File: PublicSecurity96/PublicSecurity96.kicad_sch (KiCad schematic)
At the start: 239 parts, among them J1 USB_C_Receptacle_USB2.0, U1 XC6206PxxxMR, U2 SRV05-4, U3 RP2040, Y1 16MHz

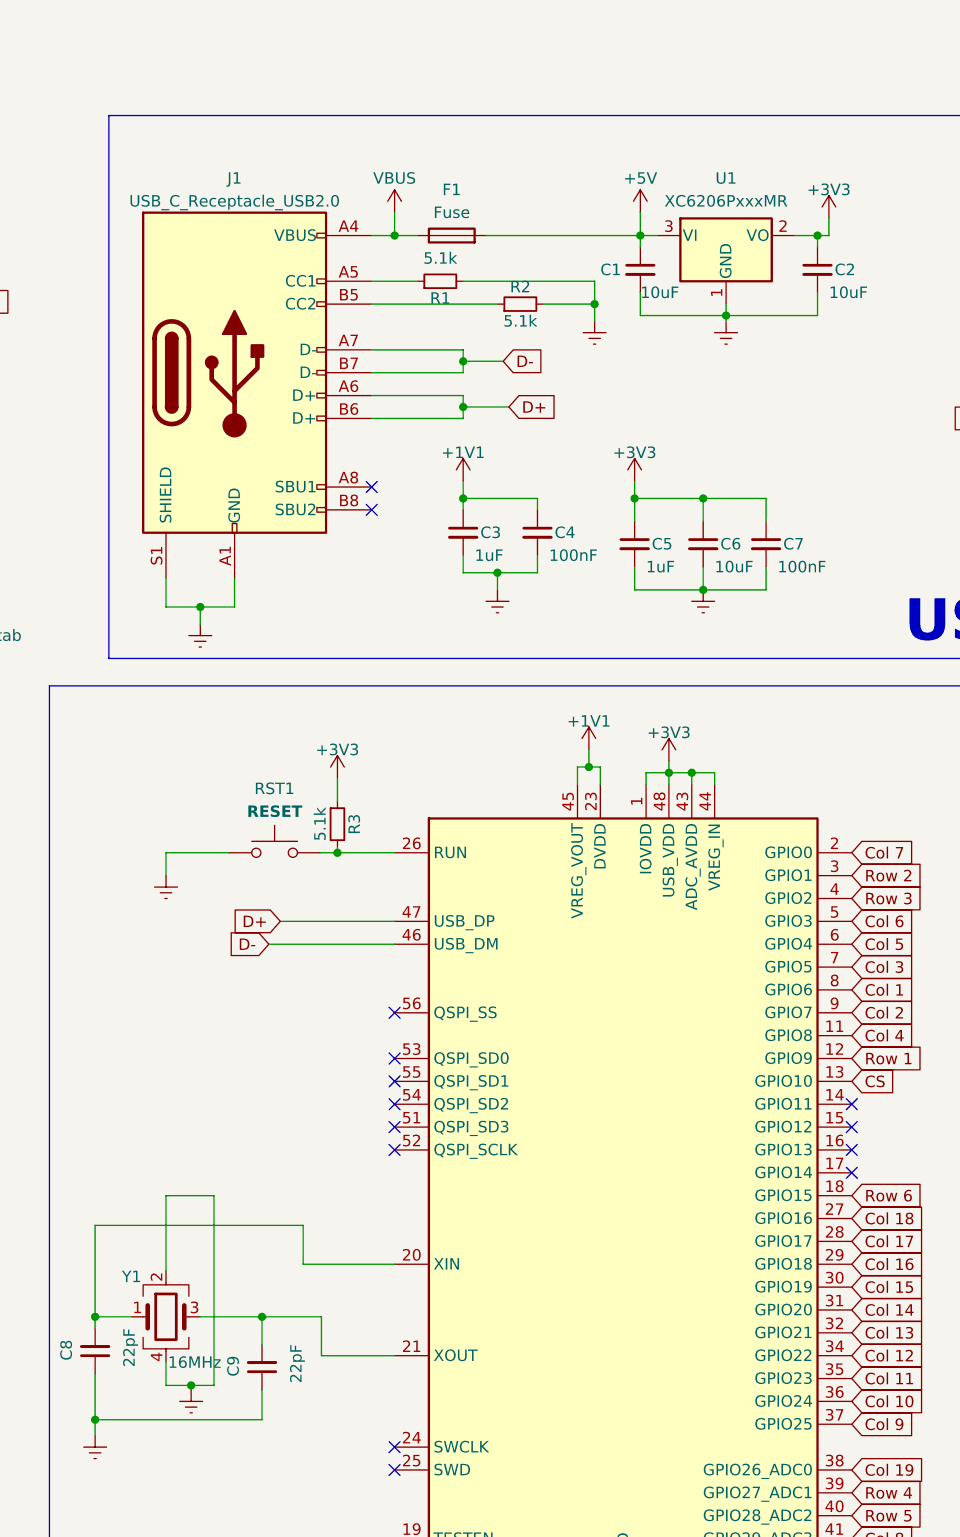
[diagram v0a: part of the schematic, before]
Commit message: kicad: swap U1 XC6206 -> AMS1117-3.3 (SOT-223 + C6186)
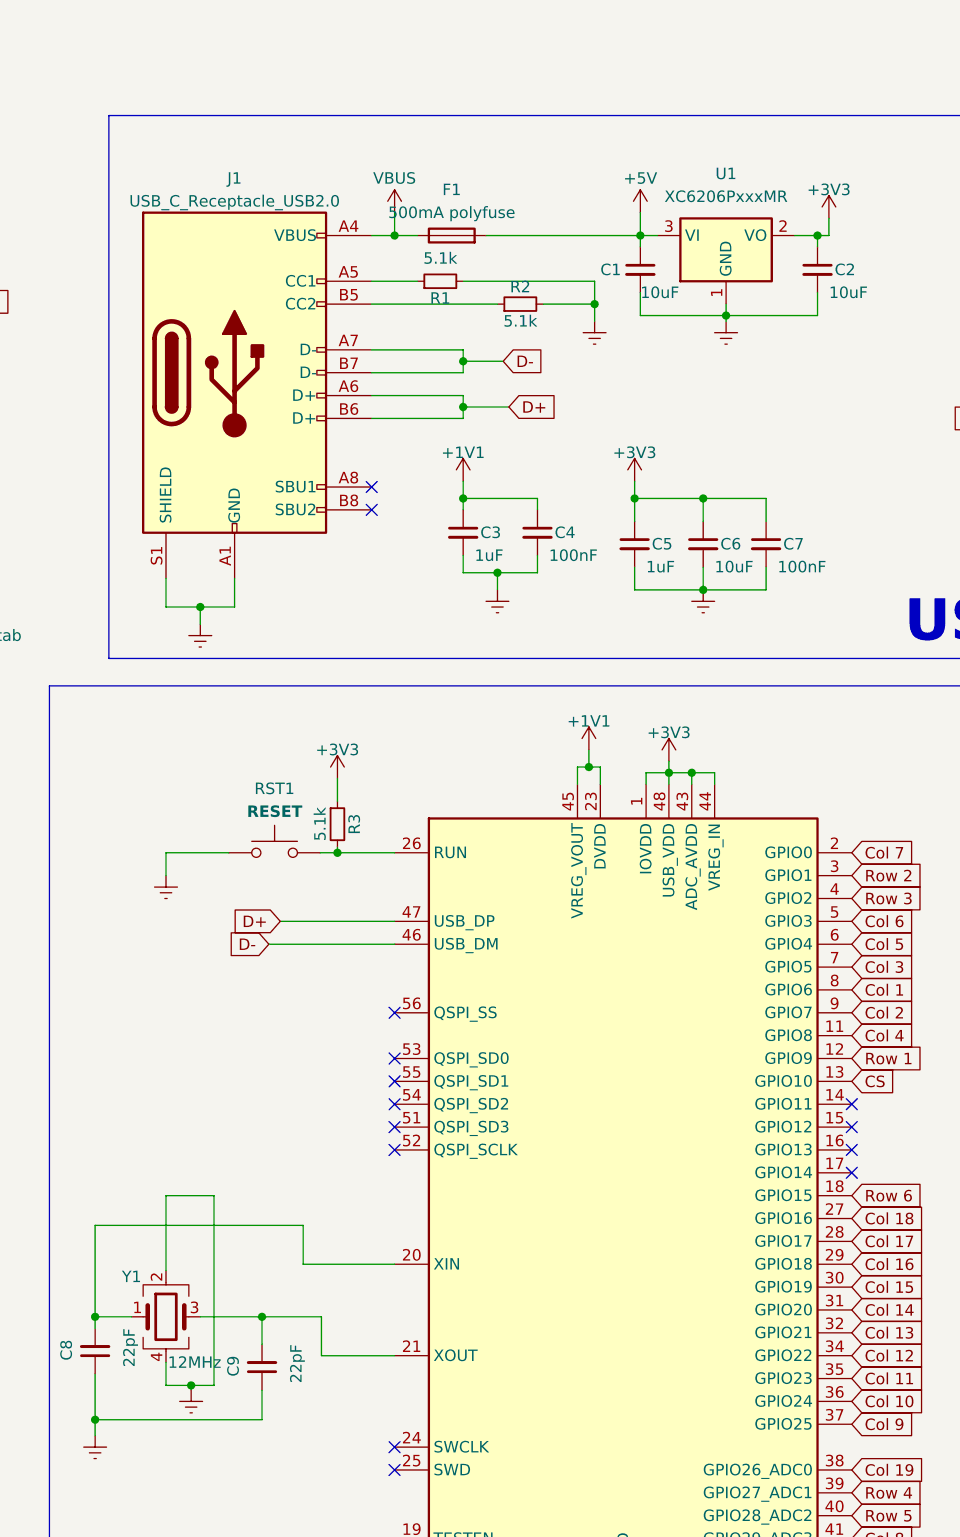
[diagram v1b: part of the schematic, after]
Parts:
- F1: value Fuse -> 500mA polyfuse; Comment 6V 500mA 100mA 1A 0805 Resettable Fuses ROHS -> 6V 500mA hold / 1A trip 1206 Resettable Polyfuse — VERIFY f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; JLCPCB part# C3035895 -> C2685389
- U1: symbol Regulator_Linear:XC6206PxxxMR -> Regulator_Linear:AMS1117-3.3; JLCPCB part# C15850 -> C6186
- Y1: value 16MHz -> 12MHz; Comment 8MHz 12pF ±10ppm SMD3225-4P Crystals ROHS -> 12MHz 12pF ±10ppm SMD3225-4P Crystals ROHS — VERIFY JLCPCB 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
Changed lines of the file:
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@@
 			)
 		)
-		(property "Value" "Fuse"
+		(property "Value" "500mA polyfuse"
 			(at 443.738 99.568 90)
 			(show_name no)
@@
 			)
 		)
-		(property "JLCPCB part#" " C3035895"
+		(property "JLCPCB part#" "C2685389"
 			(at 443.738 102.108 90)
 			(hide yes)
@@
 			)
 		)
-		(property "Comment" " 6V 500mA 100mA 1A 0805 Resettable Fuses ROHS"
+		(property "Comment" "6V 500mA hold / 1A trip 1206 Resettable Polyfuse — VERIFY footprint matches before fab"
 			(at 443.738 102.108 90)
 			(hide yes)
@@
 			)
 		)
-		(property "Value" "16MHz"
+		(property "Value" "12MHz"
 			(at 415.163 227.33 0)
 			(show_name no)
@@
 			)
 		)
-		(property "Comment" " 8MHz 12pF ±10ppm SMD3225-4P Crystals ROHS"
+		(property "Comment" " 12MHz 12pF ±10ppm SMD3225-4P Crystals ROHS — VERIFY JLCPCB part is 12MHz"
 			(at 411.988 222.25 0)
 			(hide yes)
@@
 	)
 	(symbol
-		(lib_id "Regulator_Linear:XC6206PxxxMR")
+		(lib_id "Regulator_Linear:AMS1117-3.3")
 		(at 474.218 102.108 0)
 		(unit 1)
@@
 		(fields_autoplaced yes)
 		(property "Reference" "U1"
-			(at 474.218 95.758 0)
+			(at 474.218 95.25 0)
 			(show_name no)
 			(do_not_autoplace no)
@@
 		)
 		(property "Value" "XC6206PxxxMR"
-			(at 474.218 98.298 0)
+			(at 474.218 97.79 0)
 			(show_name no)
 			(do_not_autoplace no)
@@
 		)
 		(property "Footprint" "Package_TO_SOT_SMD:SOT-223-3_TabPin2"
-			(at 474.218 96.393 0)
+			(at 474.218 97.028 0)
 			(hide yes)
 			(show_name no)
@@
 				(font
 					(size 1.27 1.27)
-					(italic yes)
 				)
 			)
 		)
-		(property "Datasheet" "https://www.torexsemi.com/file/xc6206/XC6206.pdf"
-			(at 474.218 102.108 0)
+		(property "Datasheet" "http://www.advanced-monolithic.com/pdf/ds1117.pdf"
+			(at 476.758 108.458 0)
 			(hide yes)
 			(show_name no)
@@
 			)
 		)
-		(property "Description" "Positive 60-250mA Low Dropout Regulator, Fixed Output, SOT-23"
+		(property "Description" "1A Low Dropout regulator, positive, 3.3V fixed output, SOT-223"
 			(at 474.218 102.108 0)
 			(hide yes)
@@
 			)
 		)
-		(property "JLCPCB part#" "C15850"
+		(property "JLCPCB part#" "C6186"
 			(at 474.218 102.108 0)
 			(hide yes)

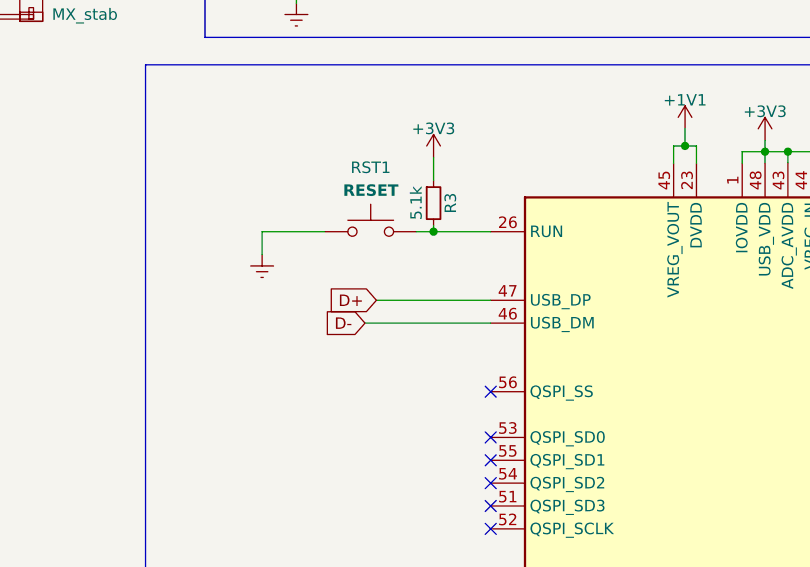
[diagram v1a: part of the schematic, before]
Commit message: wip: place R20 27R on D+ (right-pad snap to pin 47 pending)
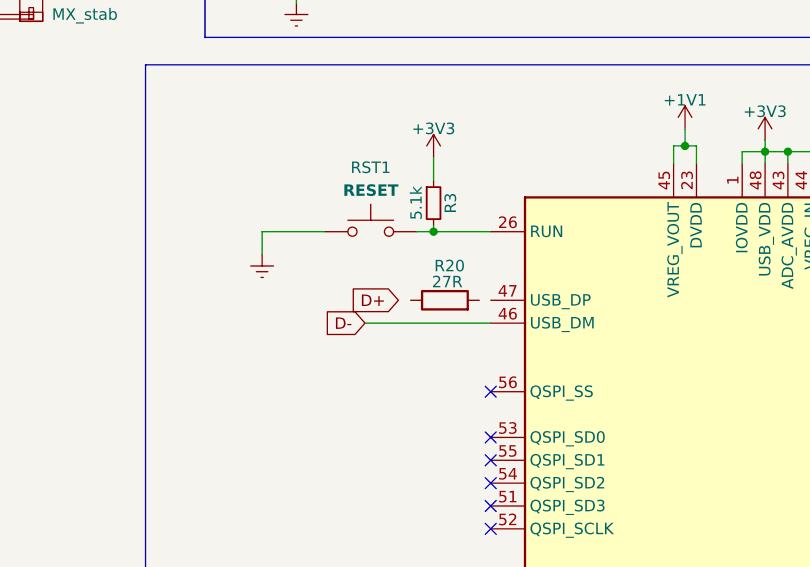
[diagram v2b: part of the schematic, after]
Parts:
- added R20: 27R, Resistor_SMD:R_0402_1005Metric, symbol Device:R
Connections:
- net D+: no longer U3.47 (USB_DP)
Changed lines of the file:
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@@
 		)
 	)
-	(wire
-		(pts
-			(xy 424.688 178.308) (xy 437.388 178.308)
-		)
-		(stroke
-			(width 0)
-			(type default)
-		)
-	)
 	(polyline
 		(pts
@@
 	(global_label "D+"
 		(shape input)
-		(at 424.688 178.308 180)
+		(at 427.1303 178.308 180)
 		(fields_autoplaced yes)
 		(effects
@@
 		)
 		(property "Intersheetrefs" "${INTERSHEET_REFS}"
-			(at 418.9398 178.308 0)
+			(at 421.3821 178.308 0)
 			(hide yes)
 			(show_name no)
@@
 					(unit 1)
 				)
+			)
+		)
+	)
+	(symbol
+		(lib_id "Device:R")
+		(at 432.2982 178.308 90)
+		(unit 1)
+		(body_style 1)
+		(exclude_from_sim no)
+		(in_bom yes)
+		(on_board yes)
+		(in_pos_files yes)
+		(dnp no)
+		(property "Reference" "R20"
+			(at 432.816 174.498 90)
+			(show_name no)
+			(do_not_autoplace no)
+			(effects
+				(font
+					(size 1.27 1.27)
+				)
+			)
+		)
+		(property "Value" "27R"
+			(at 432.562 176.276 90)
+			(show_name no)
+			(do_not_autoplace no)
+			(effects
+				(font
+					(size 1.27 1.27)
+				)
+			)
+		)
+		(property "Footprint" "Resistor_SMD:R_0402_1005Metric"
+			(at 432.2982 180.086 90)
+			(hide yes)
+			(show_name no)
+			(do_not_autoplace no)
+			(effects
+				(font
+					(size 1.27 1.27)
+				)
+			)
+		)
+		(property "Datasheet" ""
+			(at 432.2982 178.308 0)
+			(hide yes)
+			(show_name no)
+			(do_not_autoplace no)
+			(effects
+				(font
+					(size 1.27 1.27)
+				)
+			)
+		)
+		(property "Description" "Resistor"
+			(at 432.2982 178.308 0)
+			(hide yes)
+			(show_name no)
+			(do_not_autoplace no)
+			(effects
+				(font
+					(size 1.27 1.27)
+				)
+			)
+		)
+		(property "JLPCB part#" "C25092"
+			(at 432.2982 178.308 90)
+			(hide yes)
+			(show_name no)
+			(do_not_autoplace no)
+			(effects
+				(font
+					(size 1.27 1.27)
+				)
+			)
+		)
+		(pin "2"
+		)
+		(pin "1"
+		)
+		(instances
+			(project "PublicSecurity96"
+				(path "/a8aad140-1f70-470c-8dc9-e21a56e3133a"
+					(reference "R20")
+					(unit 1)
+				)
